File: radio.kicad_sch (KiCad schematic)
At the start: 1 part, among them U2 SX1276

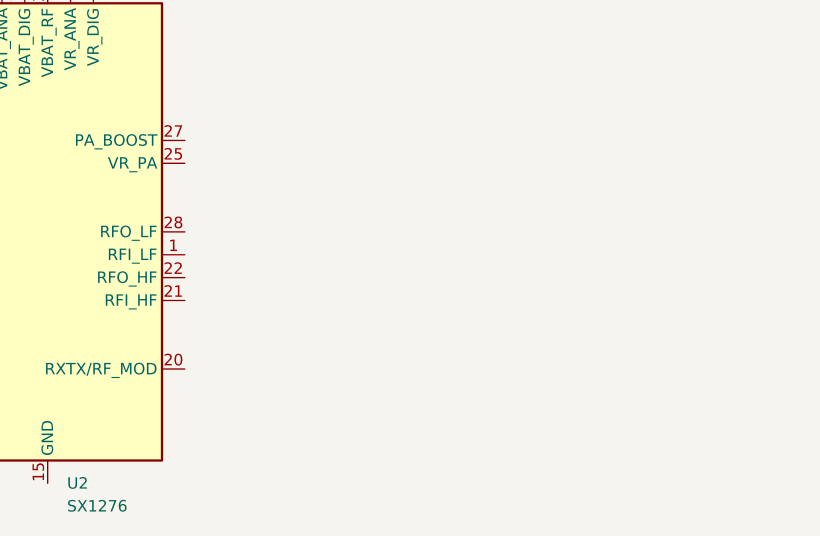
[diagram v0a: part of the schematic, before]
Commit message: copying radio from altium
copying radio from altium
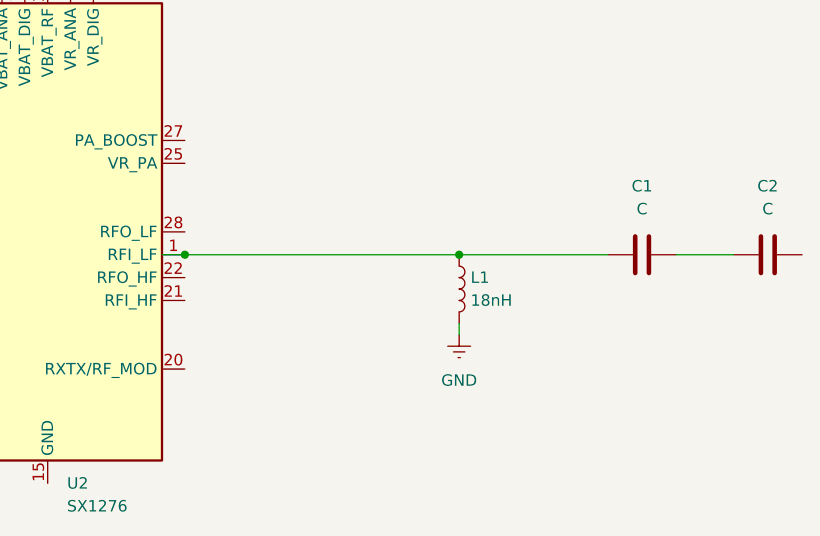
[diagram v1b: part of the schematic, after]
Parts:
- added C1, C2: C, symbol Device:C
- added L1: 18nH, symbol Device:L
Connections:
- net at U2.1 (RFI_LF): now also C1.1, L1.1
- new net: C1.2, C2.1
- new net GND: L1.2

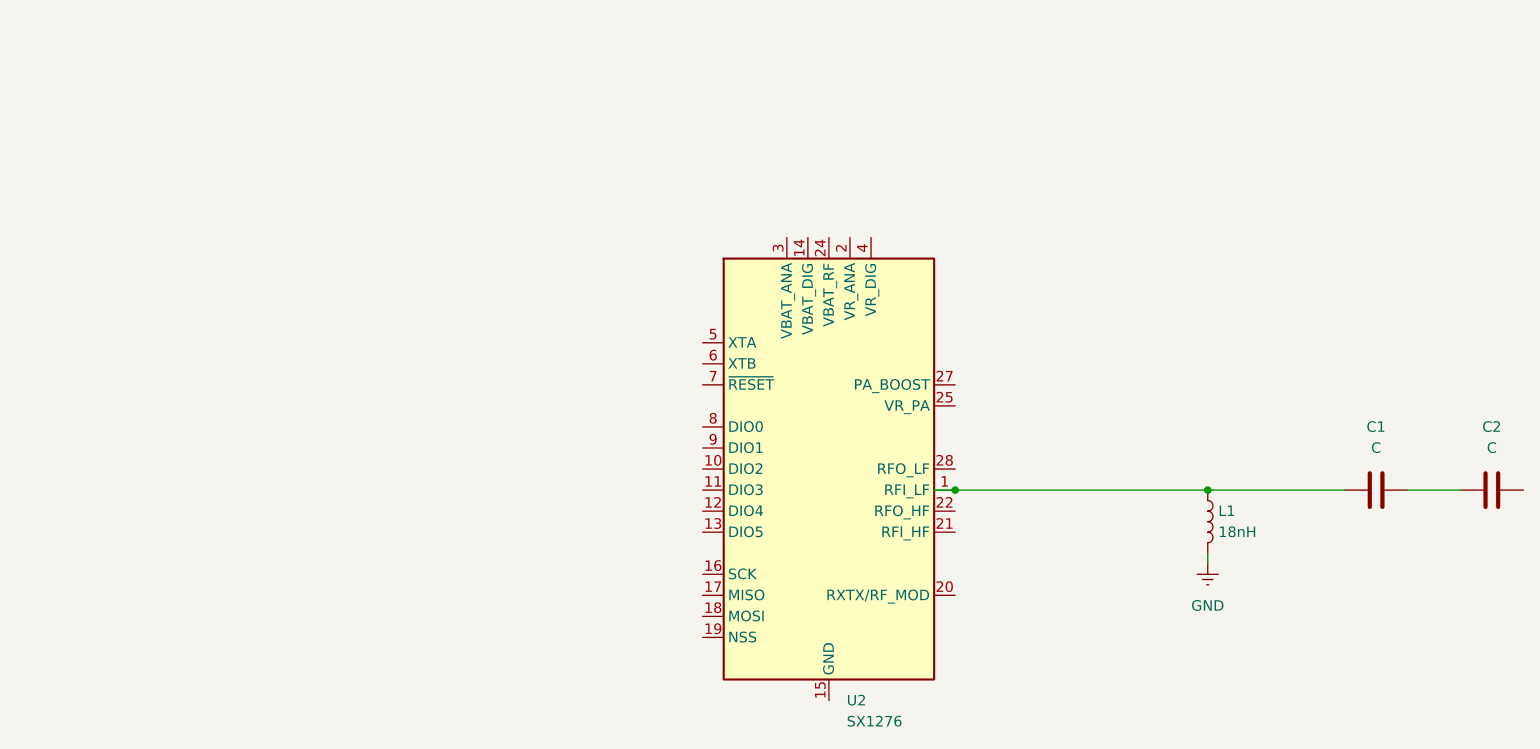
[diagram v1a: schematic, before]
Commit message: Update radio.kicad_sch
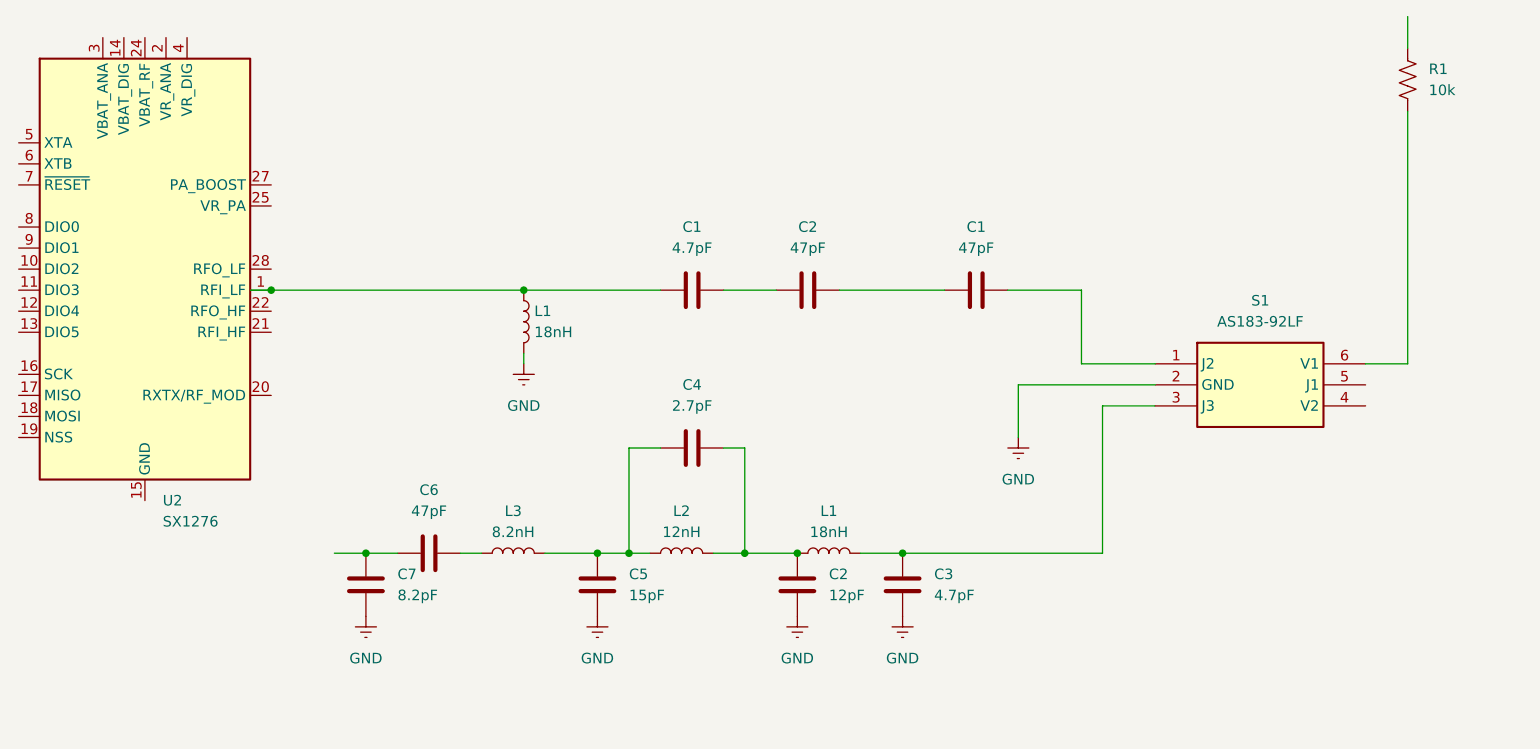
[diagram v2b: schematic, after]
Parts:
- added C1, C6: 47pF, symbol Device:C
- added C2: 12pF, symbol Device:C
- added C3: 4.7pF, symbol Device:C
- added C4: 2.7pF, symbol Device:C
- added C5: 15pF, symbol Device:C
- added C7: 8.2pF, symbol Device:C
- added L1: 18nH, symbol Device:L
- added L2: 12nH, symbol Device:L
- added L3: 8.2nH, symbol Device:L
- added R1: 10k, symbol Device:R_US
- added S1: AS183-92LF, SOT65P220X110-6N, symbol AS183-92LF:AS183-92LF
- C1: value C -> 4.7pF
- C2: value C -> 47pF
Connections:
- net GND: now also C2.2, C3.2, C5.2, C7.2, S1.2 (GND)
- net at C2.2: now also C1.1
- new net: R1.2, S1.6 (V1)
- new net: C2.1, C4.2, L1.1, L2.2
- new net: C3.1, L1.2, S1.3 (J3)
- new net: C4.1, C5.1, L2.1, L3.2
- new net: C6.1, C7.1
- new net: C6.2, L3.1
- new net: C1.2, S1.1 (J2)
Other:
- moved on the sheet: C1, C2, L1, U2

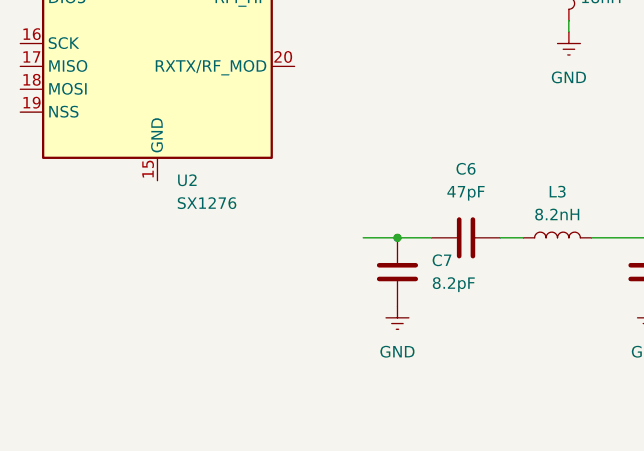
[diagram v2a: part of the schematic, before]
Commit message: Update radio.kicad_sch
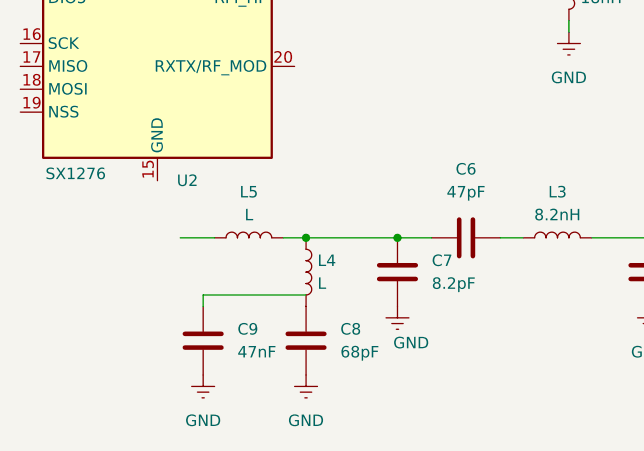
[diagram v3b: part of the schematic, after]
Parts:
- added C8: 68pF, symbol Device:C
- added C9: 47nF, symbol Device:C
- added L4, L5: L, symbol Device:L
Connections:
- net GND: now also C8.2, C9.2
- net at C6.1, C7.1: now also L4.1, L5.2
- new net: C8.1, L4.2

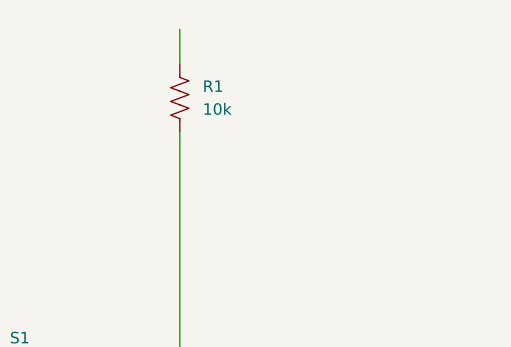
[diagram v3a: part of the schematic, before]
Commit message: Update radio.kicad_sch
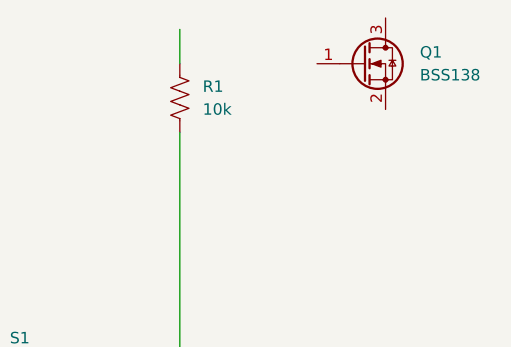
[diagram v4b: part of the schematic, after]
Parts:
- added Q1: BSS138, Package_TO_SOT_SMD:SOT-23, symbol Transistor_FET:BSS138
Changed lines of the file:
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@@
+	)
+	(symbol
+		(lib_id "Transistor_FET:BSS138")
+		(at 237.49 39.37 0)
+		(unit 1)
+		(exclude_from_sim no)
+		(in_bom yes)
+		(on_board yes)
+		(dnp no)
+		(fields_autoplaced yes)
+		(property "Reference" "Q1"
+			(at 243.84 38.0999 0)
+			(effects
+				(font
+					(size 1.27 1.27)
+				)
+				(justify left)
+			)
+		)
+		(property "Value" "BSS138"
+			(at 243.84 40.6399 0)
+			(effects
+				(font
+					(size 1.27 1.27)
+				)
+				(justify left)
+			)
+		)
+		(property "Footprint" "Package_TO_SOT_SMD:SOT-23"
+			(at 242.57 41.275 0)
+			(effects
+				(font
+					(size 1.27 1.27)
+					(italic yes)
+				)
+				(justify left)
+				(hide yes)
+			)
+		)
+		(property "Datasheet" "https://www.onsemi.com/pub/Collateral/BSS138-D.PDF"
+			(at 242.57 43.18 0)
+			(effects
+				(font
+					(size 1.27 1.27)
+				)
+				(justify left)
+				(hide yes)
+			)
+		)
+		(property "Description" "50V Vds, 0.22A Id, N-Channel MOSFET, SOT-23"
+			(at 237.49 39.37 0)
+			(effects
+				(font
+					(size 1.27 1.27)
+				)
+				(hide yes)
+			)
+		)
+		(pin "1"
+		)
+		(pin "3"
+		)
+		(pin "2"
+		)
+		(instances
+			(project ""
+				(path "/b9b95eea-71d5-442b-8957-d665de7a4ab9"
+					(reference "Q1")
+					(unit 1)
+				)
+			)
+		)
 	)
 	(symbol

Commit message: finished radio schematic
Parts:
- removed C1, C3: 4.7pF, symbol Device:C
- removed C1, C2, C6: 47pF, symbol Device:C
- removed C2: 12pF, symbol Device:C
- removed C4: 2.7pF, symbol Device:C
- removed C5: 15pF, symbol Device:C
- removed C7: 8.2pF, symbol Device:C
- removed C8: 68pF, symbol Device:C
- removed C9: 47nF, symbol Device:C
- removed L1 (x2): 18nH, symbol Device:L
- removed L2: 12nH, symbol Device:L
- removed L3: 8.2nH, symbol Device:L
- removed L4, L5: L, symbol Device:L
- removed Q1: BSS138, Package_TO_SOT_SMD:SOT-23, symbol Transistor_FET:BSS138
- removed R1: 10k, symbol Device:R_US
- removed S1: AS183-92LF, SOT65P220X110-6N, symbol AS183-92LF:AS183-92LF
- removed U2: SX1276, Package_DFN_QFN:QFN-28-1EP_6x6mm_P0.65mm_EP4.8x4.8mm, symbol RF:SX1276
- added C?: 12pF, FP-GRM155-0_05-MFG, symbol Altium Content Vault:root_0_b4654b650e69147ec39a6b967a45e02_Altium Content Vault
- added C? (x6): 100nF, FP-C0603C-CF-MFG, symbol Altium Content Vault:root_0_b4654b650e69147ec39a6b967a45e02_Altium Content Vault
- added C? (x3): 8.2pF, FP-GJM155-0_05-MFG, symbol Altium Content Vault:root_0_02cd4be3c70576c341d710602a673aa_Altium Content Vault
- added C? (x3): 47pF, CAPC1005X55X25LL05T10, symbol Altium Content Vault:root_0_CAP_Altium Content Vault_0
- added C?: 4.7pF, FP-GRM155-0_05-MFG, symbol Altium Content Vault:root_0_11868f565c42a9108669ba33697ecf6_Altium Content Vault
- added C?: 15pF, FP-GJM155-0_05-MFG, symbol Altium Content Vault:root_0_02cd4be3c70576c341d710602a673aa_Altium Content Vault
- added C?: 68pF, CAPC1005X55X25ML05T10, symbol Altium Content Vault:root_1_CAP_Altium Content Vault_0
- added C?: 2.7pF, CAPC1005X55X25ML05T10, symbol Altium Content Vault:root_0_CAP_Altium Content Vault_0
- added C?: 10nF, FP-C1608-080-0_1-MFG, symbol Altium Content Vault:root_3_mirrored_236180d848d6139a670b325ea6854c9_Altium Con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
- added C?: 10nF, FP-C1608-080-0_1-MFG, symbol Altium Content Vault:root_0_mirrored_236180d848d6139a670b325ea6854c9_Altium Con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
- added C?: 47nF, FP-GRM155-0_05-IPC_C, symbol Altium Content Vault:root_0_02cd4be3c70576c341d710602a673aa_Altium Content Vault
- added C?: 4.7pF, FP-GRM155-0_05-MFG, symbol Altium Content Vault:root_1_11868f565c42a9108669ba33697ecf6_Altium Content Vault
- added C?: 68pF, CAPC1005X55X25ML05T10, symbol Altium Content Vault:root_0_CAP_Altium Content Vault_0
- added L?: 56nH, FP-LQW15AN_80-MFG, symbol Altium Content Vault:root_3_725321dda6339637d4d059423bc1c3c_Altium Content Vault
- added L?: 12nH, FP-LQW15AN_00-W0_6-0_1-MFG, symbol Altium Content Vault:root_0_725321dda6339637d4d059423bc1c3c_Altium Content Vault
- added L?: 18nH, FP-LQW15AN_00-W0_6-0_1-MFG, symbol Altium Content Vault:root_1_725321dda6339637d4d059423bc1c3c_Altium Content Vault
- added L?: 4.7nH, FP-LQW15AN_00-W0_6-0_1-MFG, symbol Altium Content Vault:root_0_725321dda6339637d4d059423bc1c3c_Altium Content Vault
- added L? (x2): 18nH, FP-LQW15AN_00-W0_6-0_1-MFG, symbol Altium Content Vault:root_0_725321dda6339637d4d059423bc1c3c_Altium Content Vault
- added L?: 8.2nH, FP-LQW15AN_00-W0_6-0_1-MFG, symbol Altium Content Vault:root_0_725321dda6339637d4d059423bc1c3c_Altium Content Vault
- added LORA?: 60312242114510, 60312242114510, symbol Altium Content Vault:root_0_Jack_4GND_Altium Content Vault
- added Q?: BSS138W-7-F, DIOD-SOT323-3_V, symbol Altium Content Vault:root_3_mirrored_NEMOS-GSD-3_Altium Content Vault
- added R?: 10k, FP-RT0603-MFG, symbol Altium Content Vault:root_1_1029c3af85768c4190bb7ad29bc67b5_Altium Content Vault
- added U? (x2): SX1276IMLTRT, SMTC-QFN-28_V, symbol Altium Content Vault:root_0_SMTC-SX127X-QFN-28_Altium Content Vault
- added X?: AS183-92LF, SOT65P220X110-6N, symbol Purdue Space Program - High Altitude:root_0_AS183-92LF_Purdue Space Program - H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
- added Y?: ECS-TXO-25CSMV-320-AM-TR, C__Users_Public_Documents_SnapEDA Altium Plugin_libraries_SnapEDA_Library_ECS-TXO-25CSMV-320-AM-TR.PcbLib:OSC_ECS-2520S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, symbol *:root_0_ECS-TXO-25CSMV-320-AM-TR_*
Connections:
- net GND: now also C?.1, C?.1, C?.2, C?.2, C?.2, C?.2, C?.2, C?.2, C?.2, C?.2, C?.2, C?.2, C?.2, C?.2, C?.2, L?.1, LORA?.2 (GND), LORA?.3 (GND), LORA?.4 (GND), LORA?.5 (GND), Q?.2 (S), U?.15 (GND), U?.23 (GND), U?.26 (GND), U?.29 (GND), X?.2 (GND), Y?.1 (TRI_STATE), Y?.2 (GND)
- new net: C?.1, U?.2 (VR_ANA)
- new net: C?.1, U?.4 (VR_DIG)
- new net: C?.2, X?.1 (J2)
- new net: C?.1, L?.2, X?.3 (J3)
- new net: C?.1, X?.5 (J1)
- new net: Q?.3 (D), R?.1, X?.6 (V1)
- new net: C?.1, C?.2, L?.1, L?.2
- new net: C?.1, C?.1, L?.1, L?.2 (x2)
- new net: C?.1, L?.2, U?.1 (RFI_LF)
- new net: C?.1, C?.2, U?.5 (XTA), Y?.3 (OUTPUT)
- new net: C?.1, C?.2, L?.1
- new net: C?.2, L?.1
- new net: C?.1, L?.2, LORA?.1 (Signal)
- new net: C?.1, C?.2 (x2)
- new net 3V3: C?.1, C?.1, C?.1, C?.1, C?.2, R?.2, U?.14 (VBAT_DIG), U?.24 (VBAT_RF), U?.3 (VBAT_ANA), Y?.4 (VDD)
- new net CS: U?.19 (NSS)
- new net LORA_RXTX: Q?.1 (G), U?.20 (RXTX/RF_MOD), X?.4 (V2)
- new net MISO: U?.17 (MISO)
- new net MOSI: U?.18 (MOSI)
- new net NRST_WL: U?.7 (NRESET)
- new net PA_BOOST: L?.1, U?.27 (PA_BOOST)
- new net SCK: U?.16 (SCK)
- new net VR_PA: C?.1, C?.2, L?.2, U?.25 (VR_PA)
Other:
- note added: "Cuttable"

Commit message: Finish voltage regulator schematic
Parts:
- gave numbers to parts that had none: 36
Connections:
- net 3V3: now also U3.10 (DIO2/DATA), U3.8 (DIO0), U3.9 (DIO1/DCLK); no longer U3.14 (VBAT_DIG), U3.24 (VBAT_RF), U3.3 (VBAT_ANA)
- net GND: no longer U3.15 (GND), U3.23 (GND), U3.26 (GND), U3.29 (GND)
- net VR_PA: now also U3.13 (DIO5); no longer U3.25 (VR_PA)
- net at C21.1: now also U3.11 (DIO3); no longer U3.2 (VR_ANA)
- net at C22.1: now also U3.12 (DIO4); no longer U3.4 (VR_DIG)
